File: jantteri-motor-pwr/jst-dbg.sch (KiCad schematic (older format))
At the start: 1 part

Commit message: jantteri-pwr-motor
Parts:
- J3: renamed from J?; footprint (none) -> Connector_JST2:JST_ZH_B4B-ZR_1x04_P1.50mm_Vertical
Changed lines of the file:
@@
 $Descr A4 11693 8268
 encoding utf-8
-Sheet 8 8
+Sheet 7 10
 Title ""
 Date ""
@@
 GND
 $Comp
-L Connector:Conn_01x04_Male J?
+L Connector:Conn_01x04_Male J3
 U 1 1 61193048
 P 4550 3500
-F 0 "J?" H 4658 3781 50  0000 C CNN
+F 0 "J3" H 4658 3781 50  0000 C CNN
 F 1 "DBG" H 4658 3690 50  0000 C CNN
-F 2 "" H 4550 3500 50  0001 C CNN
+F 2 "Connector_JST2:JST_ZH_B4B-ZR_1x04_P1.50mm_Vertical" H 4550 3500 50  0001 C CNN
 F 3 "~" H 4550 3500 50  0001 C CNN
 	1    4550 3500

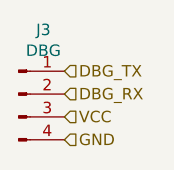
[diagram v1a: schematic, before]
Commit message: Tuubijantteri design Ordered
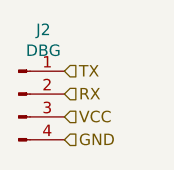
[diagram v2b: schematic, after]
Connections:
- net DBG_RX renamed RX
- net DBG_TX renamed TX
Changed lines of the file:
@@
 $Descr A4 11693 8268
 encoding utf-8
-Sheet 7 10
+Sheet 8 12
 Title ""
 Date ""
@@
 $EndDescr
 Text HLabel 4750 3400 2    50   Input ~ 0
-DBG_TX
+TX
 Text HLabel 4750 3500 2    50   Input ~ 0
-DBG_RX
+RX
 Text HLabel 4750 3700 2    50   Input ~ 0
 GND
@@
 U 1 1 61193048
 P 4550 3500
-F 0 "J3" H 4658 3781 50  0000 C CNN
+AR Path="/61237E2D/61193048" Ref="J3"  Part="1"
+AR Path="/628B1935/61193048" Ref="J2"  Part="1"
+AR Path="/628B315A/61193048" Ref="J6"  Part="1"
+F 0 "J2" H 4658 3781 50  0000 C CNN
 F 1 "DBG" H 4658 3690 50  0000 C CNN
 F 2 "Connector_JST2:JST_ZH_B4B-ZR_1x04_P1.50mm_Vertical" H 4550 3500 50  0001 C CNN
